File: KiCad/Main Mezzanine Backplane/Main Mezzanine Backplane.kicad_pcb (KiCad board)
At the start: 4 copper layers, 48 x 97 mm, 42 parts, among them J1 BB0500220F-1002C-001, J2 BB0500220F-1002C-001, J3 FPC-05FB-50PH20, J4 FPC-05FB-50PH20, J5 FPC-05FB-50PH20, J6 FPC-05FB-50PH20, J7 FPC-05FB-50PH20, U1 D1213A-04S-7, U10 D1213A-04S-7, U11 D1213A-04S-7, U12 D1213A-04S-7, U13 D1213A-04S-7, U14 D1213A-04S-7, U15 D1213A-04S-7, U16 D1213A-04S-7, U17 D1213A-04S-7, U18 D1213A-04S-7, U19 D1213A-04S-7, U2 D1213A-04S-7, U20 D1213A-04S-7, U21 D1213A-04S-7, U22 D1213A-04S-7, U23 D1213A-04S-7, U24 D1213A-04S-7, U25 D1213A-04S-7, U26 D1213A-04S-7, U3 D1213A-04S-7, U4 D1213A-04S-7, U5 D1213A-04S-7, U6 D1213A-04S-7, U7 D1213A-04S-7, U8 D1213A-04S-7, U9 D1213A-04S-7

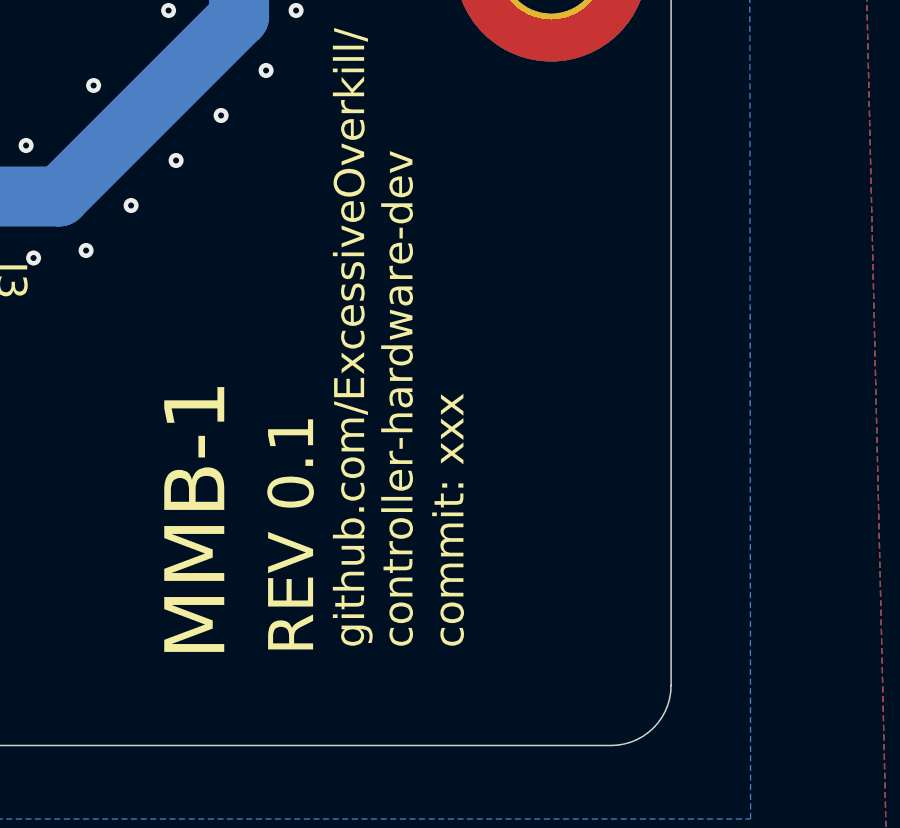
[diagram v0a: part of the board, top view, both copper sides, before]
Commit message: fix jumper
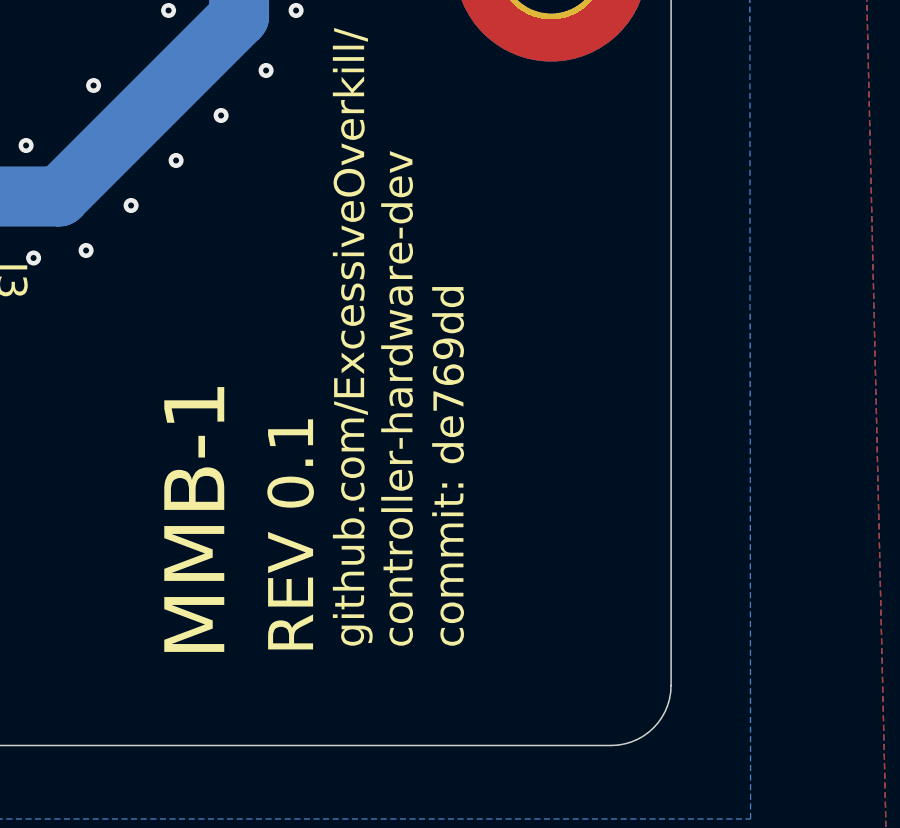
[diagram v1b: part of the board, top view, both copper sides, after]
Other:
- board text added: "commit: de769dd"
- board text removed: "commit: xxx"
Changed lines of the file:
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@@
 			(psa4output no)
 			(plotreference yes)
-			(plotvalue yes)
+			(plotvalue no)
 			(plotfptext yes)
 			(plotinvisibletext no)
@@
 			(outputformat 1)
 			(mirror no)
-			(drillshape 1)
+			(drillshape 0)
 			(scaleselection 1)
-			(outputdirectory "")
+			(outputdirectory "manufacturing outputs/")
 		)
 	)
@@
 		)
 	)
-	(gr_text "commit: xxx"
+	(gr_text "commit: de769dd"
 		(at 226.7 143.75 90)
 		(layer "F.SilkS")
